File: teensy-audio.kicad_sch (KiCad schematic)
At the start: 64 parts, among them J1 AudioJack3, J10 Conn_02x06_Odd_Even, J11 Conn_02x08_Odd_Even, J12 Barrel_Jack, J13 Conn_01x04, J2 Conn_01x06, J3 Conn_01x04, J4 Conn_02x05_Odd_Even, J5 AudioJack3, J6 Conn_01x04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

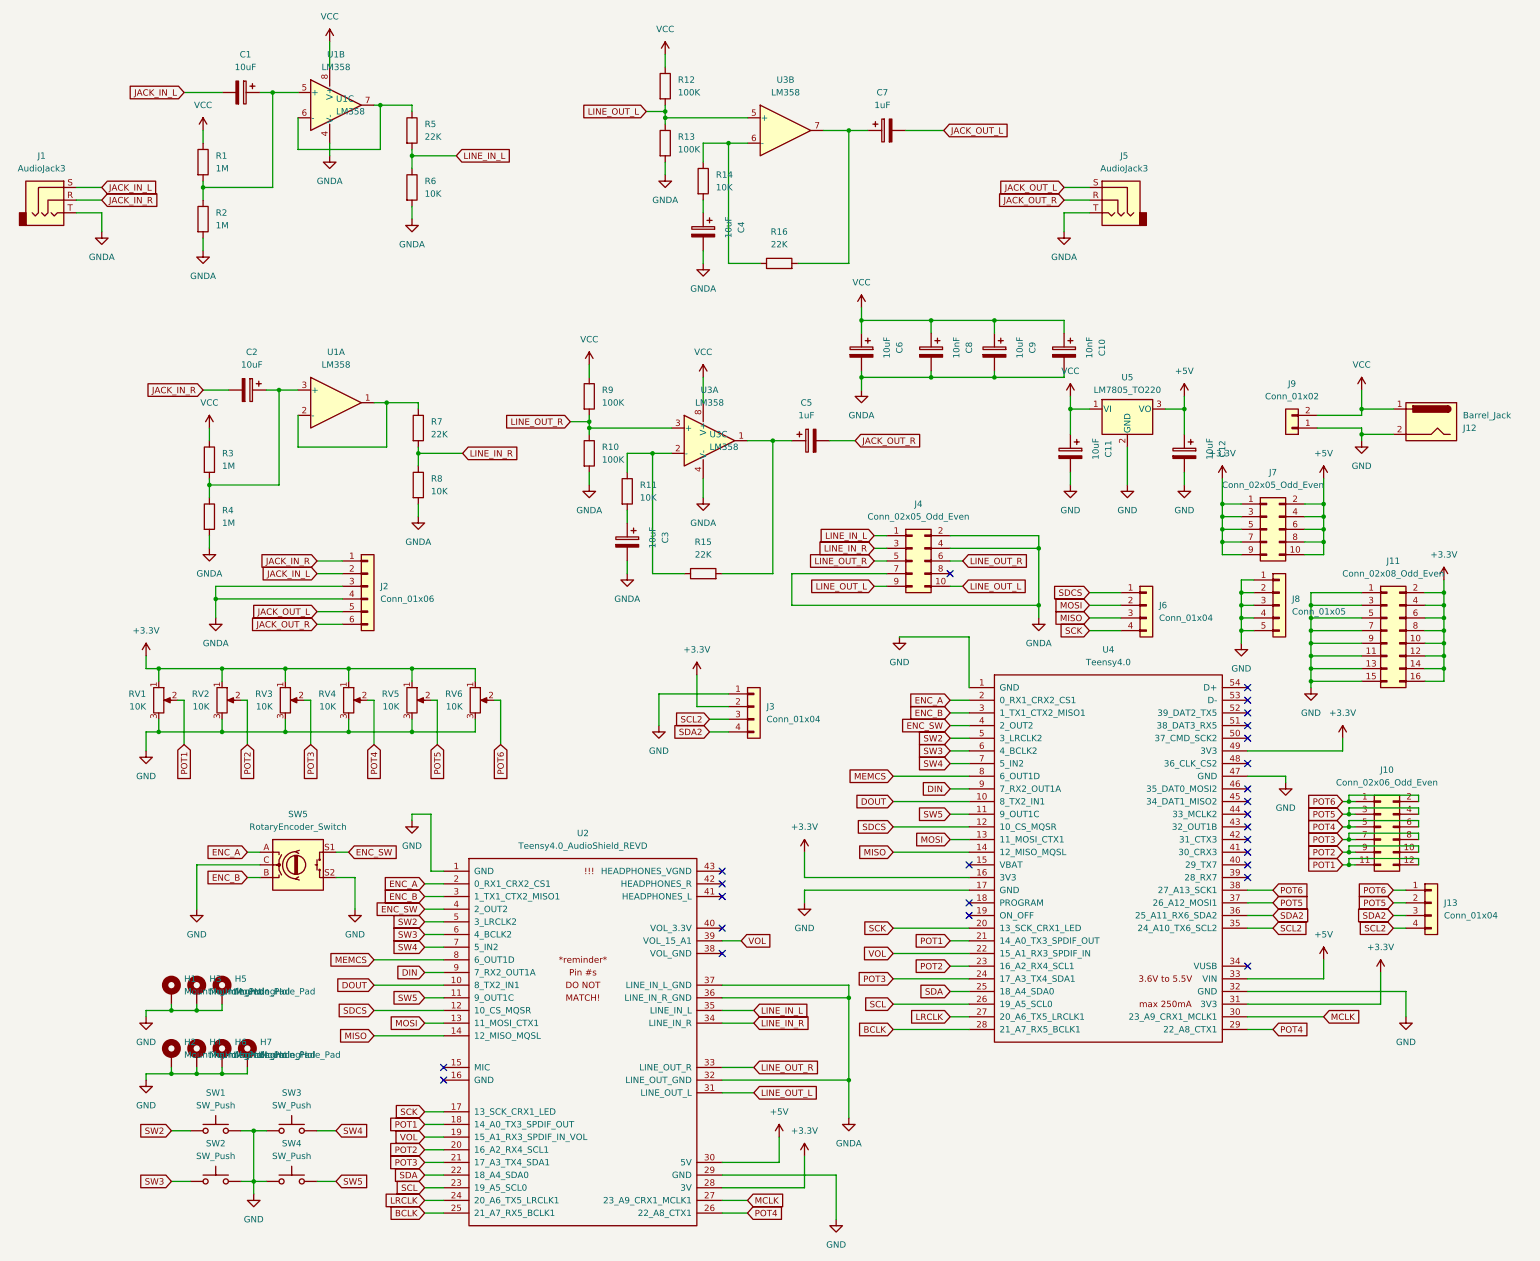
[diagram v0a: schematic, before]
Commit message: do not stack teensy and teensy audio
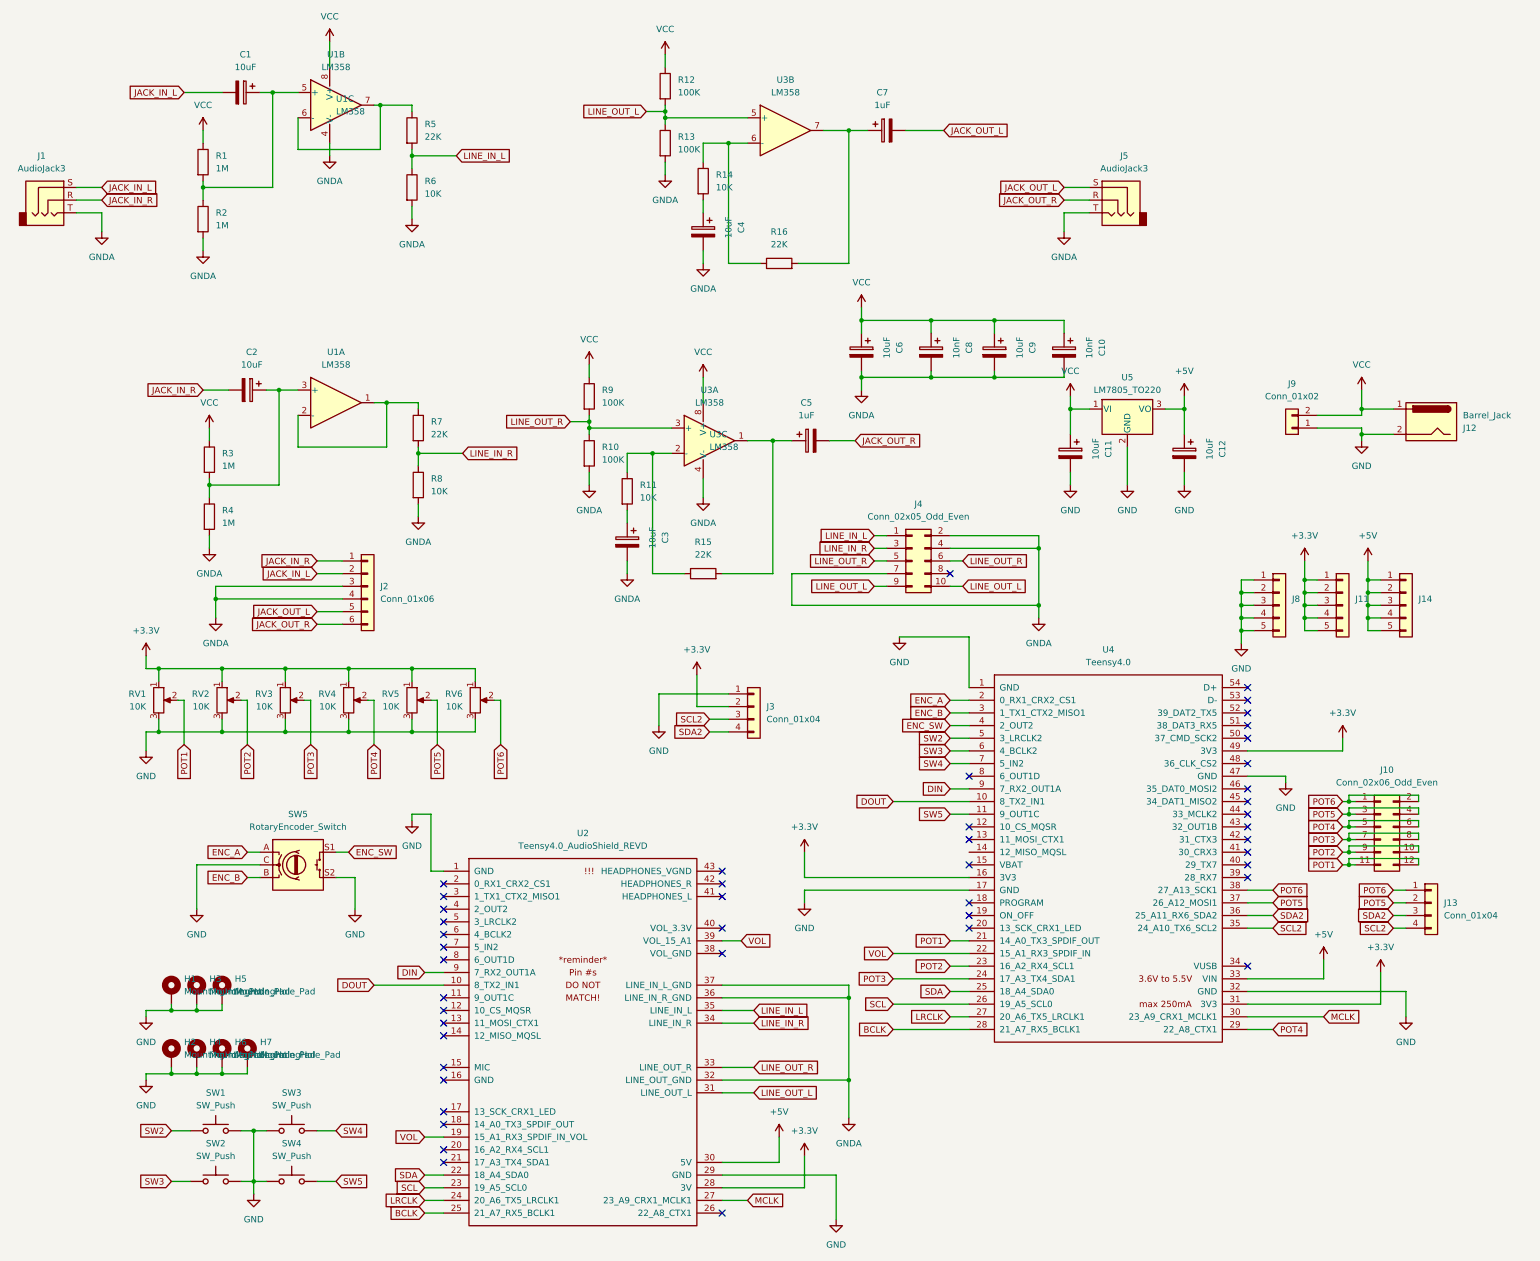
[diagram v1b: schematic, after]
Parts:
- removed J11: Conn_02x08_Odd_Even, Connector_PinHeader_2.54mm:PinHeader_2x08_P2.54mm_Vertical, symbol Connector_Generic:Conn_02x08_Odd_Even
- removed J6: Conn_01x04, Connector_PinHeader_2.54mm:PinHeader_1x04_P2.54mm_Vertical, symbol Connector_Generic:Conn_01x04
- removed J7: Conn_02x05_Odd_Even, Connector_PinHeader_2.54mm:PinHeader_2x05_P2.54mm_Vertical, symbol Connector_Generic:Conn_02x05_Odd_Even
- added J11, J14: Conn_01x05, Connector_PinHeader_2.54mm:PinHeader_1x05_P2.54mm_Vertical, symbol Connector_Generic:Conn_01x05
- H1, H3, H5: footprint MountingHole:MountingHole_4.3mm_M4_DIN965_Pad_TopBottom -> MountingHole:MountingHole_3.2mm_M3_DIN965_Pad_TopBottom
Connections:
- net +3.3V: now also J11.1 (Pin_1), J11.2 (Pin_2), J11.3 (Pin_3), J11.4 (Pin_4), J11.5 (Pin_5)
- net +5V: now also J14.1 (Pin_1), J14.2 (Pin_2), J14.3 (Pin_3), J14.4 (Pin_4), J14.5 (Pin_5)
- net ENC_A: no longer U2.2 (0_RX1_CRX2_CS1)
- net ENC_B: no longer U2.3 (1_TX1_CTX2_MISO1)
- net ENC_SW: no longer U2.4 (2_OUT2)
- net POT1: no longer U2.18 (14_A0_TX3_SPDIF_OUT)
- net POT2: no longer U2.20 (16_A2_RX4_SCL1)
- net POT3: no longer U2.21 (17_A3_TX4_SDA1)
- net POT4: no longer U2.26 (22_A8_CTX1)
- net SW2: no longer U2.5 (3_LRCLK2)
- net SW3: no longer U2.6 (4_BCLK2)
- net SW4: no longer U2.7 (5_IN2)
- net SW5: no longer U2.11 (9_OUT1C)
- net MEMCS: no longer names the net of U2.8 (6_OUT1D)
- net MEMCS: no longer U4.8 (6_OUT1D)
- net MISO: no longer names the net of U2.14 (12_MISO_MQSL)
- net MISO: no longer U4.14 (12_MISO_MQSL)
- net MOSI: no longer names the net of U2.13 (11_MOSI_CTX1)
- net MOSI: no longer U4.13 (11_MOSI_CTX1)
- net SCK: no longer names the net of U2.17 (13_SCK_CRX1_LED)
- net SCK: no longer U4.20 (13_SCK_CRX1_LED)
- net SDCS: no longer names the net of U2.12 (10_CS_MQSR)
- net SDCS: no longer U4.12 (10_CS_MQSR)
- no-connect marks 26 -> 46
